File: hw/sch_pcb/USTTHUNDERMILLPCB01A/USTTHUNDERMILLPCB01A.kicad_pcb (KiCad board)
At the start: 2 copper layers, 80 x 80 mm, 64 parts, among them J1 SM04B-GHS-TB, J2 SM04B-GHS-TB, J3 HEADER_2x01_PARALLEL, J4 HEADER_2x03, J5 SM08B-GHS-TB, J6 SM06B-GHS-TB, U1 ISL21080DIH312Z-TK 1V25, U2 OPA314, U3 MIC5504-3.3YM5, U4 PCF8583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

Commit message: Import Openscad exports
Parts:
- U5: moved to B.Cu
- moved U8 163.9 mm to (160.3, 98.7)
- moved JP1 147.5 mm to (152.9, 110.3)
- moved U7 128.1 mm to (139.7, 108.0)
- moved J6 117.9 mm to (111.2, 100.3)
- moved U5 113.3 mm to (136.8, 76.8)
- moved J5 112.4 mm to (94.5, 94.8)
- moved U2 101.3 mm to (127.9, 91.3)
- moved C2 90.4 mm to (123.3, 92.3)
- moved C1 72.2 mm to (12.1, -21.1)
- moved C10 72.2 mm to (-43.2, 22.7)
- moved C11 72.2 mm to (-25.2, -17.3)
- moved C12 72.2 mm to (-12.5, -23.8)
- moved C13 72.2 mm to (-39.2, -4.87)
- moved C14 72.2 mm to (-16.7, -23.8)
- moved C15 72.2 mm to (-25.9, -14.6)
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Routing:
- net (no net): track 0.00 -> 4.08 mm
- net Net-(C2-Pad2): track 0.00 -> 2.58 mm
- net /STATOR: track 0.00 -> 2.06 mm, vias 0 -> 1
- net GND: vias 0 -> 32
- added copper zone on F.Cu, net GND
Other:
- outline, holes or cut-outs redrawn

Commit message: uprava layoutu
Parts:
- moved C2 1.71 mm to (124.5, 93.5)
- moved U2 0.93 mm to (128.8, 91.6)
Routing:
- net GND: vias 32 -> 31
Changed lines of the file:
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@@
   )
   (footprint "Package_TO_SOT_SMD:SOT-23-5" (layer "F.Cu")
-    (at 127.9144 91.3384)
+    (at 128.8089 91.6076)
     (descr "SOT, 5 Pin (https://www.jedec.org/sites/default/files/docs/Mo-178c.PDF variant AA), generated with kicad-footprint-generator ipc_gullwing_generator.py")
     (tags "SOT TO_SOT_SMD")
@@
   )
   (footprint "Mlab_R:SMD-0805" (layer "F.Cu")
-    (at 123.2535 92.3036)
+    (at 124.4981 93.472)
     (property "Sheetfile" "USTTHUNDERMILLPCB01A.kicad_sch")
     (property "Sheetname" "")
@@
   (via (at 127.311385 102.417225) (size 0.8) (drill 0.4) (layers "F.Cu" "B.Cu") (free) (net 2))
   (via (at 123.8504 78.0288) (size 0.8) (drill 0.4) (layers "F.Cu" "B.Cu") (free) (net 2))
-  (via (at 124.387662 93.494261) (size 0.8) (drill 0.4) (layers "F.Cu" "B.Cu") (free) (net 2))
   (via (at 124.576741 89.706767) (size 0.8) (drill 0.4) (layers "F.Cu" "B.Cu") (free) (net 2))
   (via (at 119.481929 87.2663) (size 0.8) (drill 0.4) (layers "F.Cu" "B.Cu") (free) (net 2))
@@
   (via (at 120.740448 83.348766) (size 0.8) (drill 0.4) (layers "F.Cu" "B.Cu") (free) (net 2))
   (via (at 128.431222 103.95054) (size 0.8) (drill 0.4) (layers "F.Cu" "B.Cu") (free) (net 2))
-  (segment (start 122.301 92.3036) (end 120.904 92.3036) (width 0.25) (layer "F.Cu") (net 3))
-  (via (at 120.904 92.3036) (size 0.8) (drill 0.4) (layers "F.Cu" "B.Cu") (net 3))
+  (segment (start 123.5456 93.3196) (end 122.7328 92.5068) (width 0.25) (layer "F.Cu") (net 3))
+  (segment (start 123.5456 93.472) (end 123.5456 93.3196) (width 0.25) (layer "F.Cu") (net 3))
+  (via (at 122.5296 92.5068) (size 0.8) (drill 0.4) (layers "F.Cu" "B.Cu") (net 3))
   (segment (start 120.904 92.3036) (end 121.5644 92.3036) (width 0.25) (layer "B.Cu") (net 3))
-  (segment (start 126.7769 92.2884) (end 124.2212 92.2884) (width 0.25) (layer "F.Cu") (net 4))
-  (segment (start 124.2212 92.2884) (end 124.206 92.3036) (width 0.25) (layer "F.Cu") (net 4))
+  (segment (start 126.365 92.5576) (end 125.4506 93.472) (width 0.25) (layer "F.Cu") (net 4))
+  (segment (start 127.6714 92.5576) (end 126.365 92.5576) (width 0.25) (layer "F.Cu") (net 4))
   (zone (net 2) (net_name "GND") (layer "F.Cu") (name "GND") (hatch edge 0.508)
     (connect_pads (clearance 0.508))
@@
     )
   )
-  (group "" (id cd238df3-4ea1-4dad-8506-c6c80ebf5cc5)
-    (members
-      7d86ff91-0d9a-46e6-95d8-2f8bd7bb6d92
-    )
-  )

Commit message: Edit PCB
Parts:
- U6: moved to B.Cu
- moved U6 174.9 mm to (135.1, 72.1)
- moved C12 126.0 mm to (41.6, 90.0)
- moved C13 126.0 mm to (14.9, 108.9)
- moved C14 126.0 mm to (37.4, 90.0)
- moved C3 126.0 mm to (66.3, 90.0)
- moved C4 126.0 mm to (57.9, 90.0)
- moved C8 126.0 mm to (28.5, 124.6)
- moved L1 126.0 mm to (22.2, 103.7)
- moved R15 126.0 mm to (14.9, 106.2)
- moved R2 126.0 mm to (62.1, 90.0)
- moved R7 126.0 mm to (20.2, 133.4)
- moved R9 126.0 mm to (23.3, 127.8)
- moved Y1 126.0 mm to (4.46, 113.5)
- moved C1 126.0 mm to (66.3, 92.7)
- moved C10 126.0 mm to (11.0, 136.4)
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
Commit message: Edit PCB
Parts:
- removed C22: 4u7, Mlab_R:SMD-0805
- removed J2: SM04B-GHS-TB, Connector_JST:JST_GH_SM04B-GHS-TB_1x04-1MP_P1.25mm_Horizontal
- removed J3: HEADER_2x01_PARALLEL, Mlab_Pin_Headers:Straight_2x01
- removed R18: 0R, Mlab_R:SMD-0805
- removed R19: -, Mlab_R:SMD-0805
- added D1: 3v3 bipolární, Diode_SMD:D_SMA, F.Cu at (130.5, 97.4)
- C1, C10, C11, C12, C13, C14, C15, C16, C17, C18, C19, C2, C20, C23, C24, C3, C4, C5, C7: footprint Mlab_R:SMD-0805 -> Capacitor_SMD:C_0603_1608Metric
- C21, C6, C9: footprint Mlab_R:SMD-0805 -> Capacitor_SMD:C_0805_2012Metric
- C8: footprint Mlab_R:SMD-0603 -> Capacitor_SMD:C_0603_1608Metric
- D4: value HLMP-K150+FIX-LED-313 -> RED; footprint Mlab_D:FIX-LED-313 -> LED_SMD:LED_0603_1608Metric
- R1, R10, R11, R12, R13, R14, R15, R2, R3, R4, R5: footprint Mlab_R:SMD-0805 -> Resistor_SMD:R_0603_1608Metric
- R6, R7, R8, R9: footprint Mlab_R:SMD-0603 -> Resistor_SMD:R_0603_1608Metric
- moved Y1 238.4 mm to (242.3, 97.2), turned to -90 degrees
- moved C23 234.3 mm to (261.3, 95.3), turned to -90 degrees
- moved C21 231.4 mm to (263.8, 95.5), turned to -90 degrees
- moved C20 228.7 mm to (236.8, 44.8), turned to -90 degrees
- moved R17 218.2 mm to (241.2, 109.8), turned to -90 degrees
- moved D2 217.6 mm to (236.4, 151.1), turned to 90 degrees
- moved U3 215.6 mm to (226.2, 151.9), turned to -90 degrees
- moved C19 215.4 mm to (233.7, 44.7), turned to -90 degrees
- moved C7 214.9 mm to (230.0, 151.3), turned to 90 degrees
- moved C16 214.9 mm to (222.6, 43.0), turned to -90 degrees
- moved C18 211.0 mm to (231.4, 44.7), turned to -90 degrees
- moved C15 209.9 mm to (238.1, 94.4)
- moved C13 206.7 mm to (210.5, 41.9), turned to 90 degrees
- moved C17 205.8 mm to (238.3, 99.7), turned to 180 degrees
- moved L1 205.2 mm to (217.7, 41.5)
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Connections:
- U9 pad 7: Net-(R18-Pad2) -> GND
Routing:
- net GND: track 0.00 -> 49.1 mm
- net (no net): track 4.08 -> 0.57 mm
- net /STATOR: track 1.96 -> 2.97 mm
- added copper zone on B.Cu, net GND

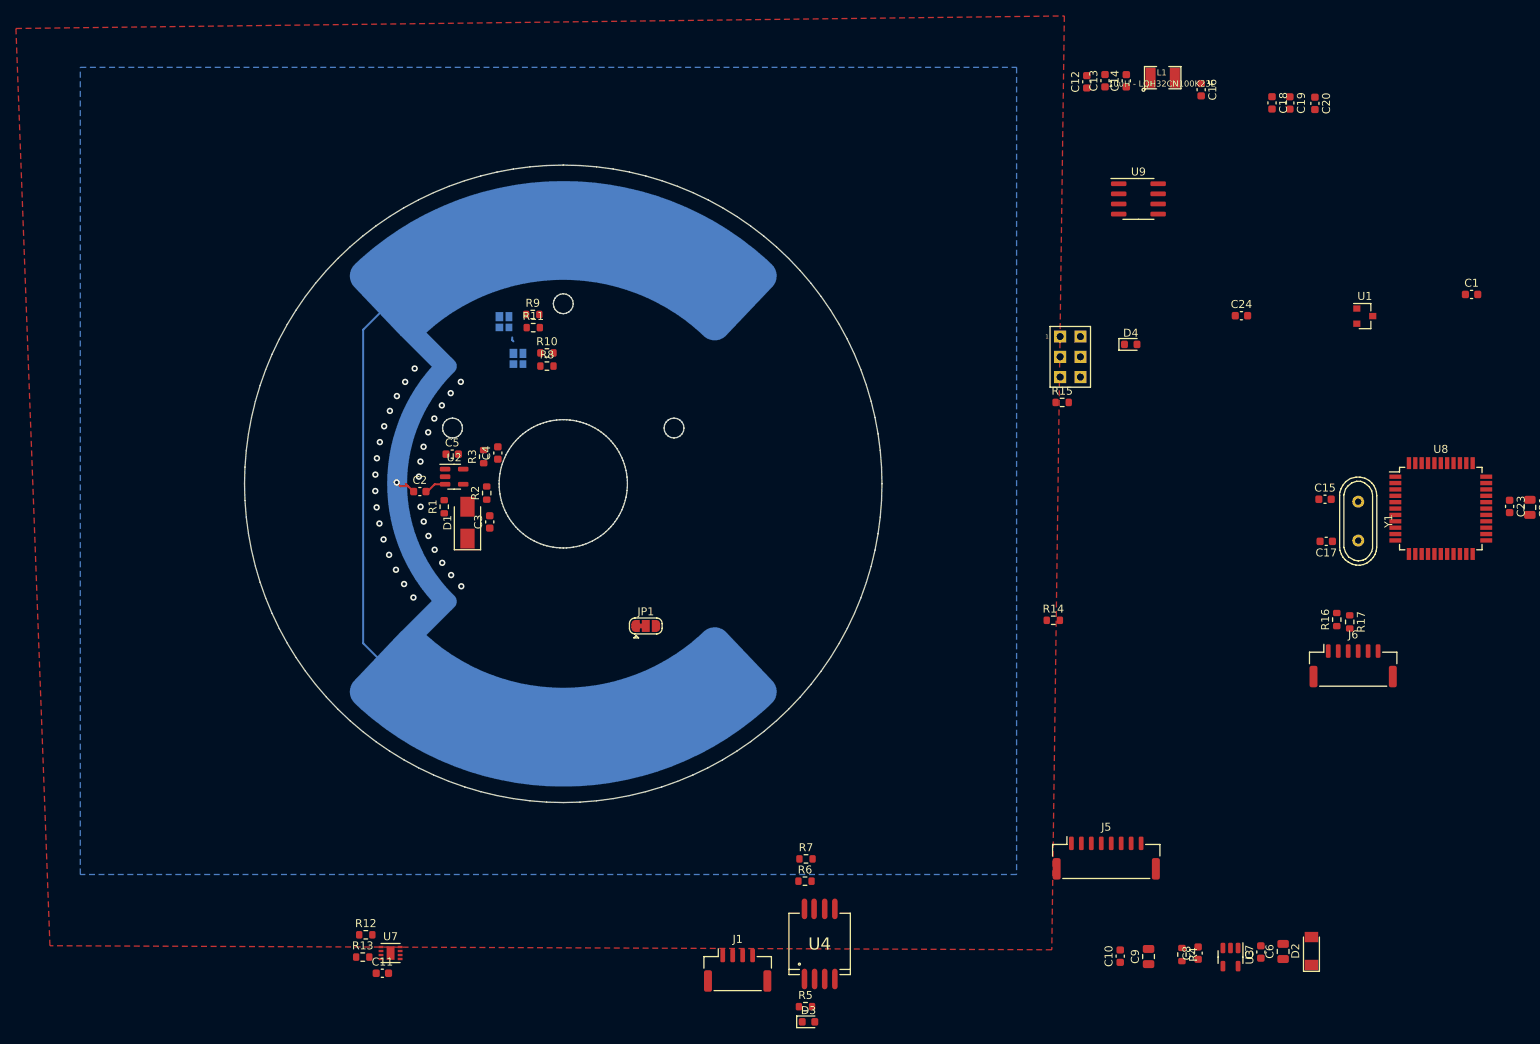
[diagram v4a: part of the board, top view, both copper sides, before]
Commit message: uprava layoutu, aktualizace elektrod
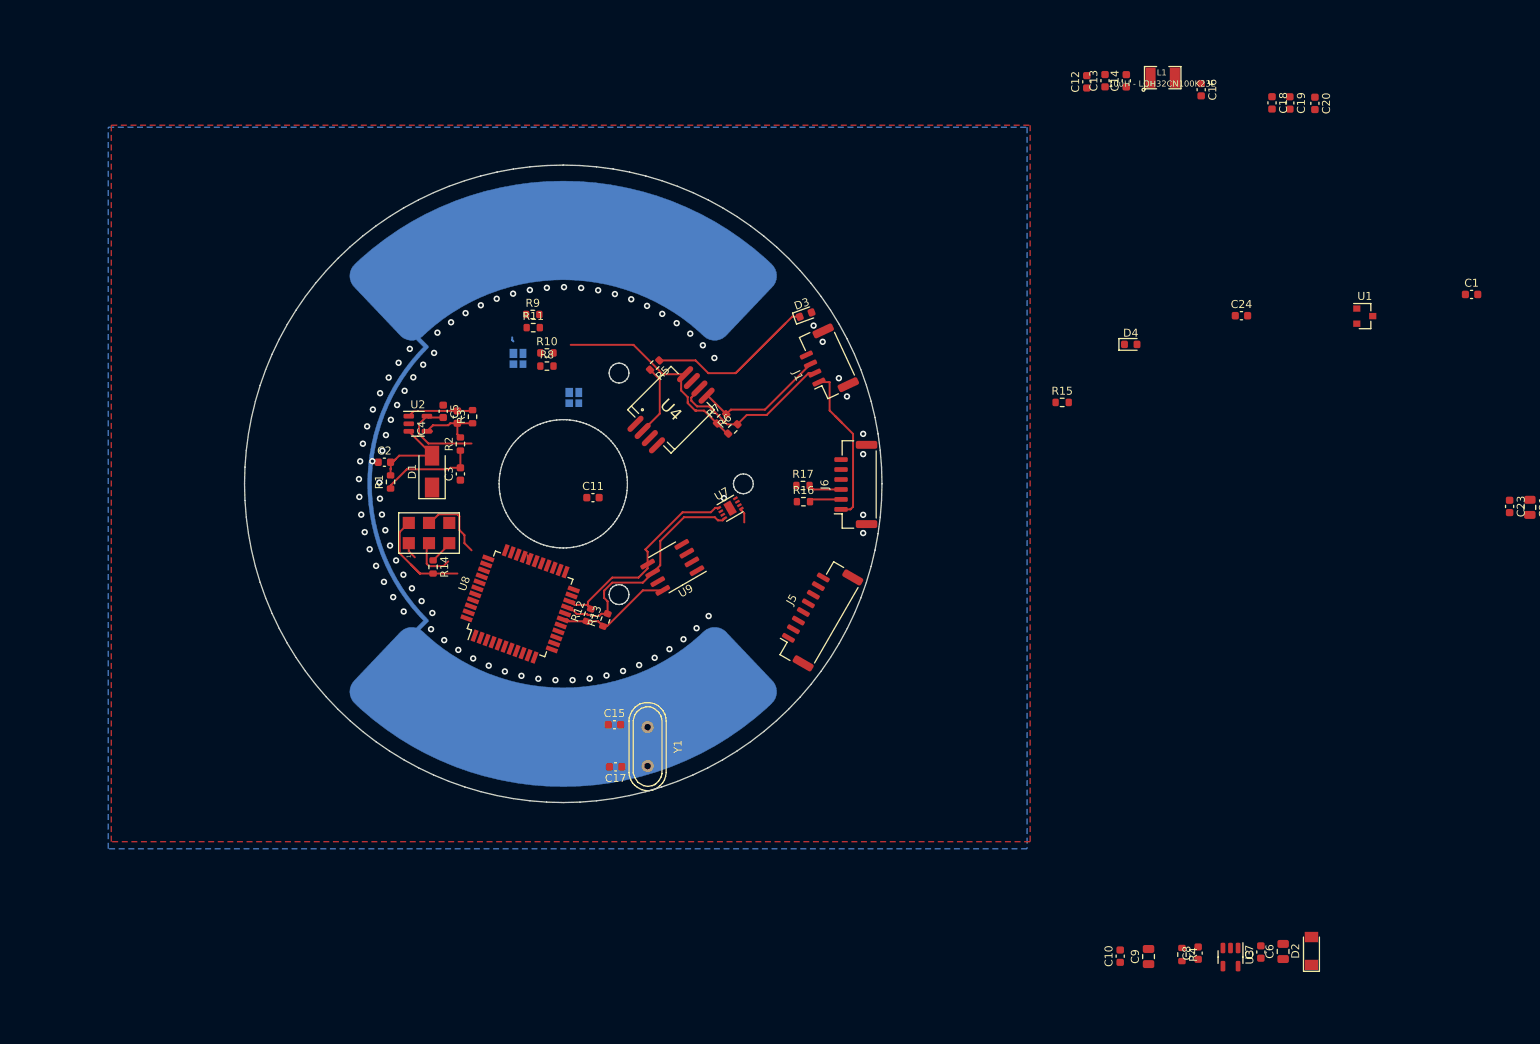
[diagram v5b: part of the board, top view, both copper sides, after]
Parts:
- removed JP1: SolderJumper_3_Bridged12, Jumper:SolderJumper-3_P1.3mm_Bridged12_RoundedPad1.0x1.5mm
- moved U8 116.2 mm to (137.1, 107.6), turned to 70 degrees
- moved C15 93.6 mm to (148.9, 122.7)
- moved C17 93.6 mm to (149.1, 128.0)
- moved Y1 93.6 mm to (153.1, 125.5)
- moved D3 88.8 mm to (172.9, 71.3), turned to 20 degrees
- moved J4 83.5 mm to (125.7, 98.7), turned to 90 degrees
- moved R5 82.7 mm to (154.0, 77.6), turned to -135 degrees
- moved R14 78.1 mm to (126.2, 102.9), turned to -90 degrees
- moved J1 77.1 mm to (175.5, 77.3), turned to 115 degrees
- moved U9 74.6 mm to (156.2, 103.0), turned to -150 degrees
- moved R17 70.7 mm to (172.6, 92.7), turned to 0 degrees
- moved U7 70.2 mm to (163.4, 95.6), turned to 30 degrees
- moved U4 69.6 mm to (156.0, 83.2), turned to -45 degrees
- moved R16 68.5 mm to (172.6, 94.7), turned to 0 degrees
- moved J6 66.4 mm to (179.2, 92.6), turned to 90 degrees
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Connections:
- U4 pad 3: Net-(JP1-Pad2) -> GND
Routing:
- net +3V3: track 0.00 -> 57.9 mm
- net GND: track 49.1 -> 0.51 mm, vias 31 -> 82
- net /CPU/PC0: track 0.00 -> 30.7 mm
- net Net-(D3-Pad1): track 0.00 -> 30.0 mm
- net /CPU/PC1: track 0.00 -> 27.4 mm
- net /tachometer/SCL: track 0.00 -> 21.3 mm
- net +5V: track 0.00 -> 21.0 mm
- net /tachometer/SDA: track 0.00 -> 16.6 mm
- net /REF_1V25: track 0.00 -> 12.2 mm
- net +3.3VP: track 0.00 -> 11.8 mm
- net Net-(C2-Pad2): track 2.60 -> 12.2 mm
- net /CPU/PB5: track 0.00 -> 9.27 mm
- net Net-(R5-Pad2): track 0.00 -> 9.09 mm
- net /PA0: track 0.00 -> 8.74 mm
- net Net-(C4-Pad1): track 0.00 -> 8.73 mm
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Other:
- outline, holes or cut-outs redrawn
